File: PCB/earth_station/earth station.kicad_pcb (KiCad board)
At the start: 2 copper layers, 25 x 50 mm, 4 parts, among them U1 ARDUPROMINI, U2 RFM95

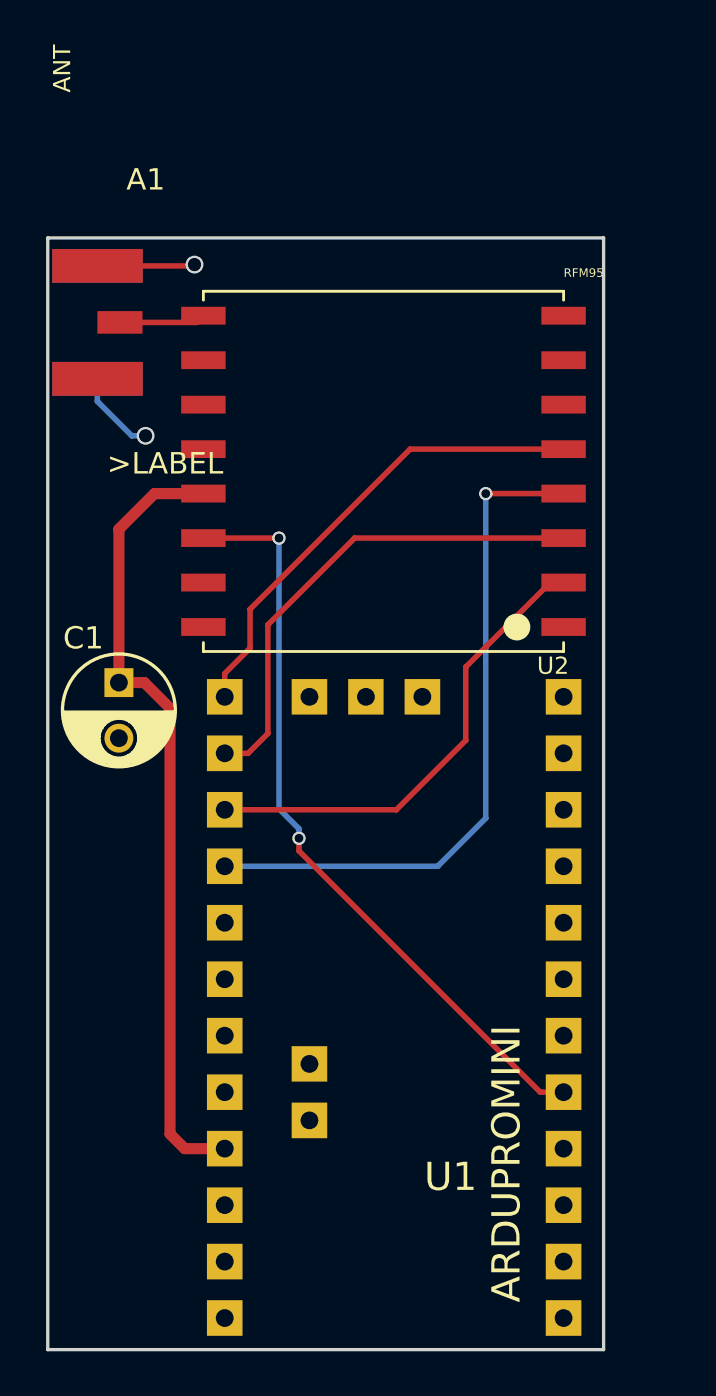
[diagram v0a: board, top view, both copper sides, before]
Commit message: Add logos
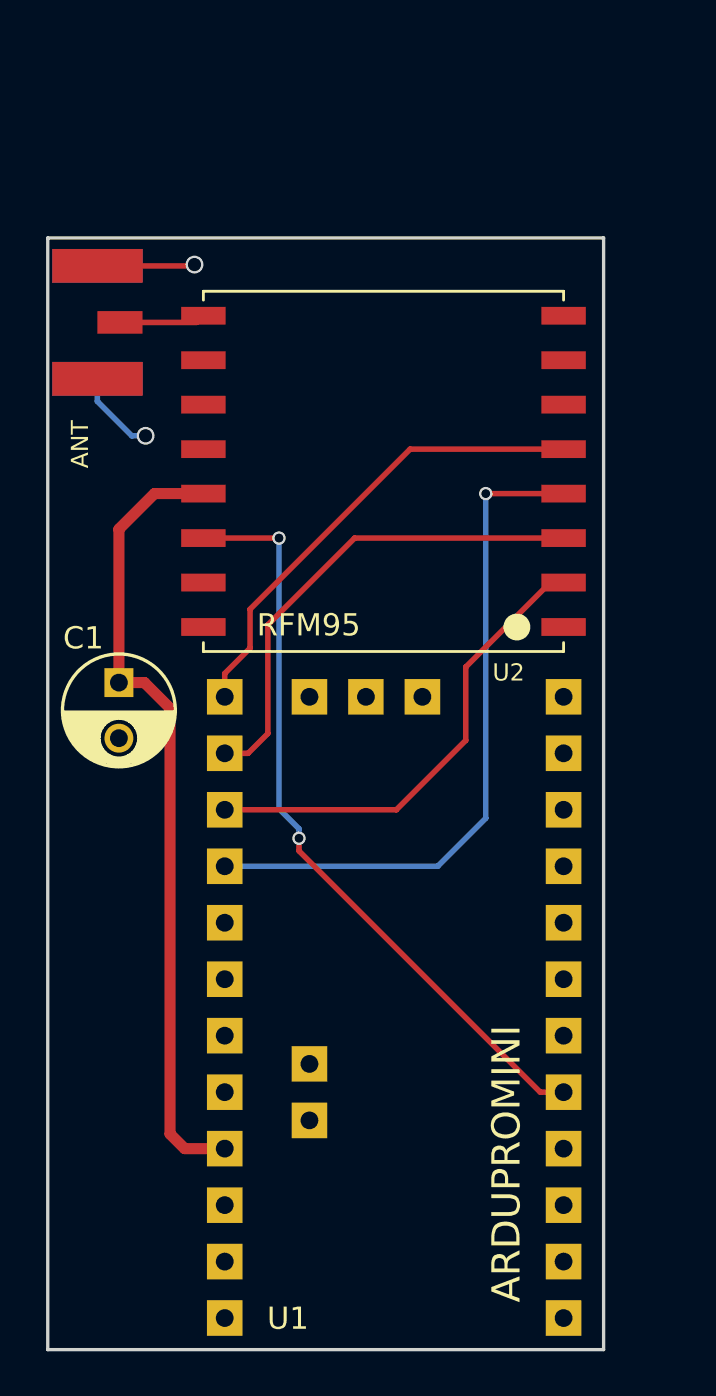
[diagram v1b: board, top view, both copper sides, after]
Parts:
- added G***: LOGO, theinventorhouse:electronic_cats_logo_8x6, B.Cu at (111.0, 100.0)
- added REF**: Symbol_OSHW-Logo_SilkScreen, Symbols:Symbol_OSHW-Logo_SilkScreen, B.Cu at (113.0, 113.8)
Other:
- board text added: "Station Board"

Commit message: Fix sma connector and pads
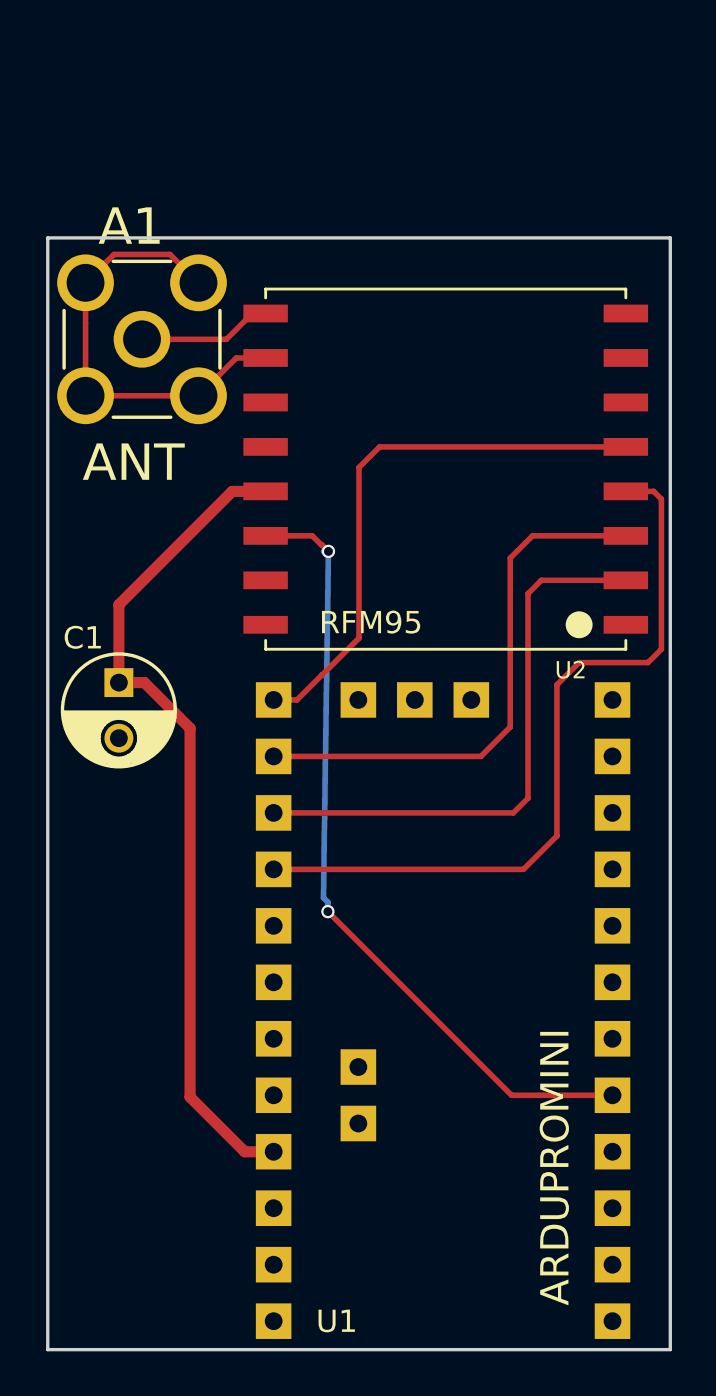
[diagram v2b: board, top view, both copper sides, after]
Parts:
- A1: footprint SMA_Conn_Ant -> smd:AMPHENOL_901-144
- moved A1 4.11 mm to (101.2, 90.6)
- moved U2 2.80 mm to (114.9, 96.4)
- moved U1 2.20 mm to (117.3, 128.4)
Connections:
- A1 pad 4: (no net) -> GND
- A1 pad 5: (no net) -> GND
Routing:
- net GND: track 4.39 -> 20.0 mm, vias 1 -> 0
- net /MISO: track 21.4 -> 25.6 mm
- net (no net): track 3.82 -> 0.00 mm, vias 1 -> 0
- net /NSS: track 21.5 -> 25.1 mm
- net /SCK: track 30.7 -> 34.0 mm, vias 1 -> 0
- net /MOSI: track 22.1 -> 24.4 mm
- net Net-(A1-Pad1): track 3.88 -> 6.04 mm
- net /INT0: track 34.2 -> 35.8 mm
- net VCC: track 36.0 -> 37.6 mm
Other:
- board size 25 x 50 mm -> 28 x 50 mm

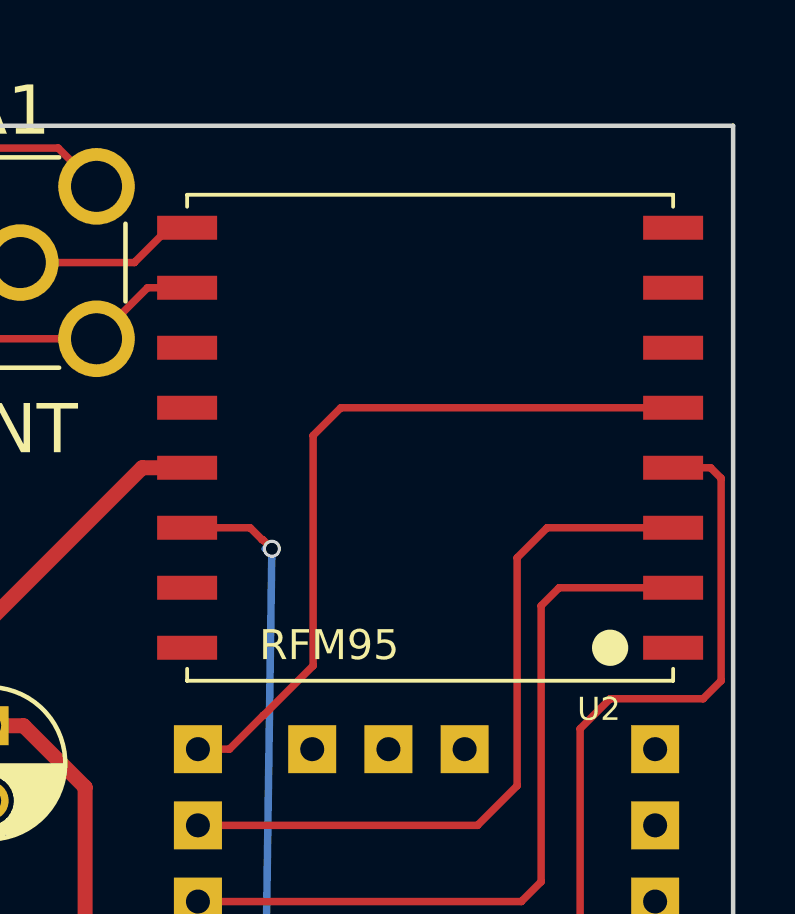
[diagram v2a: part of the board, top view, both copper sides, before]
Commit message: Update logos and fix pads
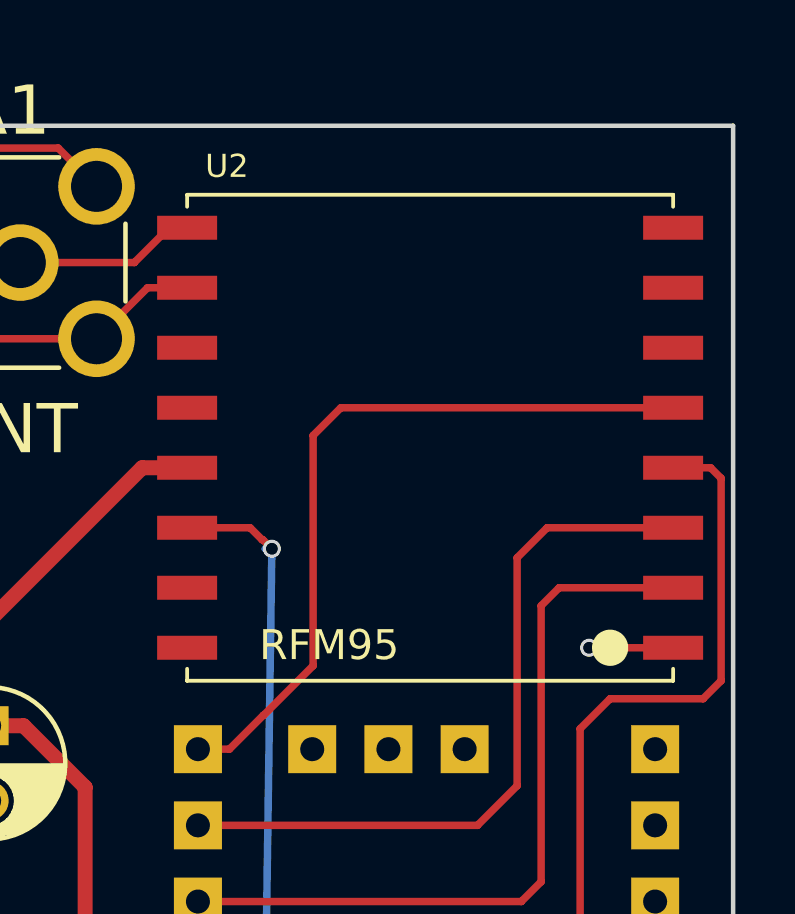
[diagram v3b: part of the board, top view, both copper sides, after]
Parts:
- moved G*** 6.00 mm to (117.0, 100.0)
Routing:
- net GND: track 20.0 -> 22.8 mm, vias 0 -> 1
- net /RST: track 0.00 -> 0.60 mm
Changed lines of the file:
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@@
-(kicad_pcb (version 4) (host pcbnew 4.0.0-rc1-stable)
+(kicad_pcb (version 4) (host pcbnew 4.0.2+dfsg1-stable)
   (general
     (links 17)
-    (no_connects 2)
+    (no_connects 5)
     (area 96.924999 85.924999 125.075001 136.075001)
     (thickness 1.6)
     (drawings 7)
-    (tracks 57)
+    (tracks 60)
     (zones 0)
     (modules 6)
@@
   (module RFM (layer F.Cu)
     (at 114.9 96.4 180)
-    (fp_text reference U2 (at -4.9 -9.5 180) (layer F.SilkS)
+    (fp_text reference U2 (at 7.5 8.6 180) (layer F.SilkS)
       (effects (font (size 0.77216 0.77216) (thickness 0.138988)) (justify left bottom))
     )
@@
   )
   (module theinventorhouse:electronic_cats_logo_8x6 (layer B.Cu)
-    (at 111 100 180)
+    (at 117 100 180)
     (fp_text reference G*** (at 0 0 180) (layer B.SilkS) hide
       (effects (font (thickness 0.3)) (justify mirror))
@@
     (arrow2b (pts (xy 97 140.2) (xy 98.126504 139.613579)))
   )
-  (gr_text "Station Board" (at 111.8 92.6) (layer B.SilkS)
+  (gr_text "Station Board" (at 115 91.4) (layer B.SilkS)
     (effects (font (size 1.5 1.5) (thickness 0.3)) (justify mirror))
   )
@@
   (segment (start 105.04 90.56) (end 106.2 89.4) (width 0.25) (layer F.Cu) (net 1))
   (segment (start 106.2 89.4) (end 106.8 89.4) (width 0.25) (layer F.Cu) (net 1))
+  (segment (start 123 103.4) (end 120.2 103.4) (width 0.25) (layer F.Cu) (net 2))
+  (via (at 120.2 103.4) (size 0.6) (drill 0.4) (layers F.Cu B.Cu) (net 2))
   (segment (start 98.7 88.02) (end 99.976349 86.743651) (width 0.25) (layer F.Cu) (net 2))
   (segment (start 99.976349 86.743651) (end 102.503651 86.743651) (width 0.25) (layer F.Cu) (net 2))
@@
   (segment (start 117.86 124.56) (end 109.6 116.3) (width 0.25) (layer F.Cu) (net 7))
   (via (at 109.6 116.3) (size 0.6) (drill 0.4) (layers F.Cu B.Cu) (net 7))
+  (segment (start 123 93.4) (end 123.6 93.4) (width 0.25) (layer F.Cu) (net 14))
   (segment (start 107.16 114.4) (end 118.4 114.4) (width 0.25) (layer F.Cu) (net 22))
   (segment (start 124 105.1) (end 124.6 104.5) (width 0.25) (layer F.Cu) (net 22))
@@
   (segment (start 107.16 109.32) (end 116.48 109.32) (width 0.25) (layer F.Cu) (net 24))
   (segment (start 111.923964 95.4) (end 123 95.4) (width 0.25) (layer F.Cu) (net 25))
+  (segment (start 111 96.323964) (end 111.923964 95.4) (width 0.25) (layer F.Cu) (net 25))
+  (segment (start 111 104) (end 111 96.323964) (width 0.25) (layer F.Cu) (net 25))
+  (segment (start 109.345001 105.654999) (end 111 104) (width 0.25) (layer F.Cu) (net 25))
+  (segment (start 109.335001 105.654999) (end 109.345001 105.654999) (width 0.25) (layer F.Cu) (net 25))
+  (segment (start 108.21 106.78) (end 109.335001 105.654999) (width 0.25) (layer F.Cu) (net 25))
   (segment (start 107.16 106.78) (end 108.21 106.78) (width 0.25) (layer F.Cu) (net 25))
-  (segment (start 108.21 106.78) (end 109.335001 105.654999) (width 0.25) (layer F.Cu) (net 25))
-  (segment (start 109.335001 105.654999) (end 109.345001 105.654999) (width 0.25) (layer F.Cu) (net 25))
-  (segment (start 109.345001 105.654999) (end 111 104) (width 0.25) (layer F.Cu) (net 25))
-  (segment (start 111 104) (end 111 96.323964) (width 0.25) (layer F.Cu) (net 25))
-  (segment (start 111 96.323964) (end 111.923964 95.4) (width 0.25) (layer F.Cu) (net 25))
   (zone (net 2) (net_name GND) (layer F.Cu) (hatch edge 0.508)
     (connect_pads (clearance 0.508))
     (min_thickness 0.254)
-    (fill yes (arc_segments 16) (thermal_gap 0.508) (thermal_bridge_width 0.508))
+    (fill (arc_segments 16) (thermal_gap 0.508) (thermal_bridge_width 0.508))
     (polygon
       (pts
@@
     (connect_pads (clearance 0.508))
     (min_thickness 0.254)
-    (fill yes (arc_segments 16) (thermal_gap 0.508) (thermal_bridge_width 0.508))
+    (fill (arc_segments 16) (thermal_gap 0.508) (thermal_bridge_width 0.508))
     (polygon
       (pts
